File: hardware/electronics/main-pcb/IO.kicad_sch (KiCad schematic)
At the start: 22 parts, among them J1 IMU1, J2 IMU2, J3 Conn_01x04_Socket, J4 XT60-M, P1 USB_C_Plug_USB2.0, SW1 PUSH

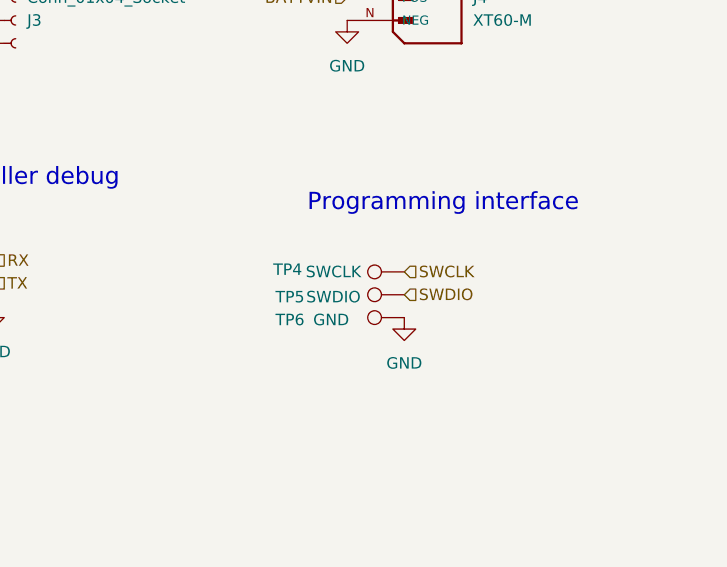
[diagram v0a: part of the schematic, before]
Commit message: worked on cmsis dap implementation aswell as cleaned up startup files for both microcontrolers
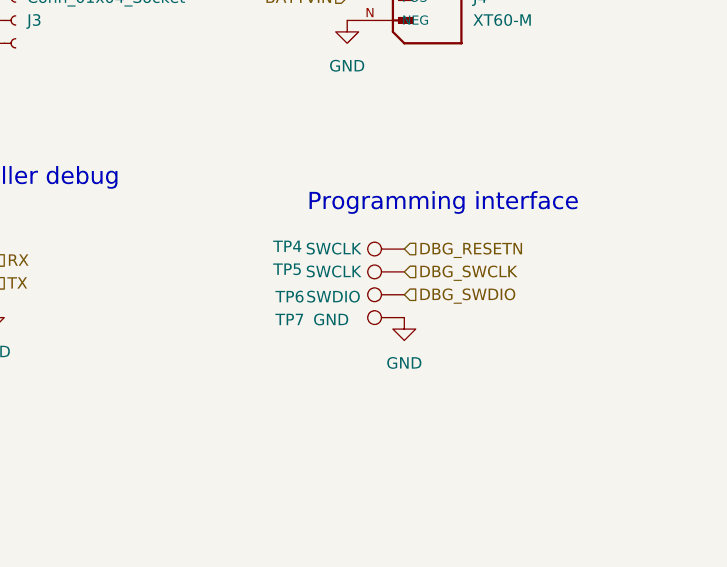
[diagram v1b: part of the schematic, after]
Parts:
- added TP4: SWCLK, TestPoint:TestPoint_Pad_D1.5mm, symbol Connector:TestPoint
- renumbered TP4 to TP5, TP5 to TP6, TP6 to TP7
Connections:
- net SWCLK renamed DBG_SWCLK
- net SWDIO renamed DBG_SWDIO
- new net DBG_RESETN: TP4.1
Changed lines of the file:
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@@
 		)
 	)
+	(hierarchical_label "DBG_RESETN"
+		(shape input)
+		(at 238.76 115.57 0)
+		(fields_autoplaced yes)
+		(effects
+			(font
+				(size 1.27 1.27)
+			)
+			(justify left)
+		)
+	)
 	(hierarchical_label "TX"
 		(shape input)
@@
 		)
 	)
-	(hierarchical_label "SWCLK"
+	(hierarchical_label "DBG_SWCLK"
 		(shape input)
 		(at 238.76 118.11 0)
@@
 		)
 	)
-	(hierarchical_label "SWDIO"
+	(hierarchical_label "DBG_SWDIO"
 		(shape input)
 		(at 238.76 120.65 0)
@@
 		(on_board yes)
 		(dnp no)
-		(property "Reference" "TP6"
+		(property "Reference" "TP7"
 			(at 226.06 123.444 90)
 			(effects
@@
 			(project "motordriver"
 				(path "/c7634e88-16d1-45ec-9aac-9c841e03cf6d/38bc72d2-c2f6-4538-9c33-e1ab2a8ac987"
-					(reference "TP6")
+					(reference "TP7")
 					(unit 1)
 				)
@@
 		(on_board yes)
 		(dnp no)
-		(property "Reference" "TP4"
+		(property "Reference" "TP5"
 			(at 225.806 117.856 90)
 			(effects
@@
 			(project "motordriver"
 				(path "/c7634e88-16d1-45ec-9aac-9c841e03cf6d/38bc72d2-c2f6-4538-9c33-e1ab2a8ac987"
-					(reference "TP4")
+					(reference "TP5")
 					(unit 1)
 				)
@@
 		(on_board yes)
 		(dnp no)
-		(property "Reference" "TP5"
+		(property "Reference" "TP6"
 			(at 226.06 120.904 90)
 			(effects
@@
 			(project "motordriver"
 				(path "/c7634e88-16d1-45ec-9aac-9c841e03cf6d/38bc72d2-c2f6-4538-9c33-e1ab2a8ac987"
-					(reference "TP5")
+					(reference "TP6")
 					(unit 1)
 				)
@@
 					(unit 1)
 				)
+			)
+		)
+	)
+	(symbol
+		(lib_id "Connector:TestPoint")
+		(at 238.76 115.57 90)
+		(unit 1)
+		(exclude_from_sim no)
+		(in_bom yes)
+		(on_board yes)
+		(dnp no)
+		(property "Reference" "TP4"
+			(at 225.806 115.316 90)
+			(effects
+				(font
+					(size 1.27 1.27)
+				)
+			)
+		)
+		(property "Value" "SWCLK"
+			(at 230.886 115.57 90)
+			(effects
+				(font
+					(size 1.27 1.27)
+				)
+			)
+		)
+		(property "Footprint" "TestPoint:TestPoint_Pad_D1.5mm"
+			(at 238.76 110.49 0)
+			(effects
+				(font
+					(size 1.27 1.27)
+				)
+				(hide yes)
+			)
+		)
+		(property "Datasheet" "~"
+			(at 238.76 110.49 0)
+			(effects
+				(font
+					(size 1.27 1.27)
+				)
+				(hide yes)
+			)
+		)
+		(property "Description" "test point"
+			(at 238.76 115.57 0)
+			(effects
+				(font
+					(size 1.27 1.27)
+				)
+				(hide yes)
+			)
+		)
+		(pin "1"
+		)
+		(instances
+			(project "motordriver"
+				(path "/c7634e88-16d1-45ec-9aac-9c841e03cf6d/38bc72d2-c2f6-4538-9c33-e1ab2a8ac987"
+					(reference "TP4")
+					(unit 1)
+				)

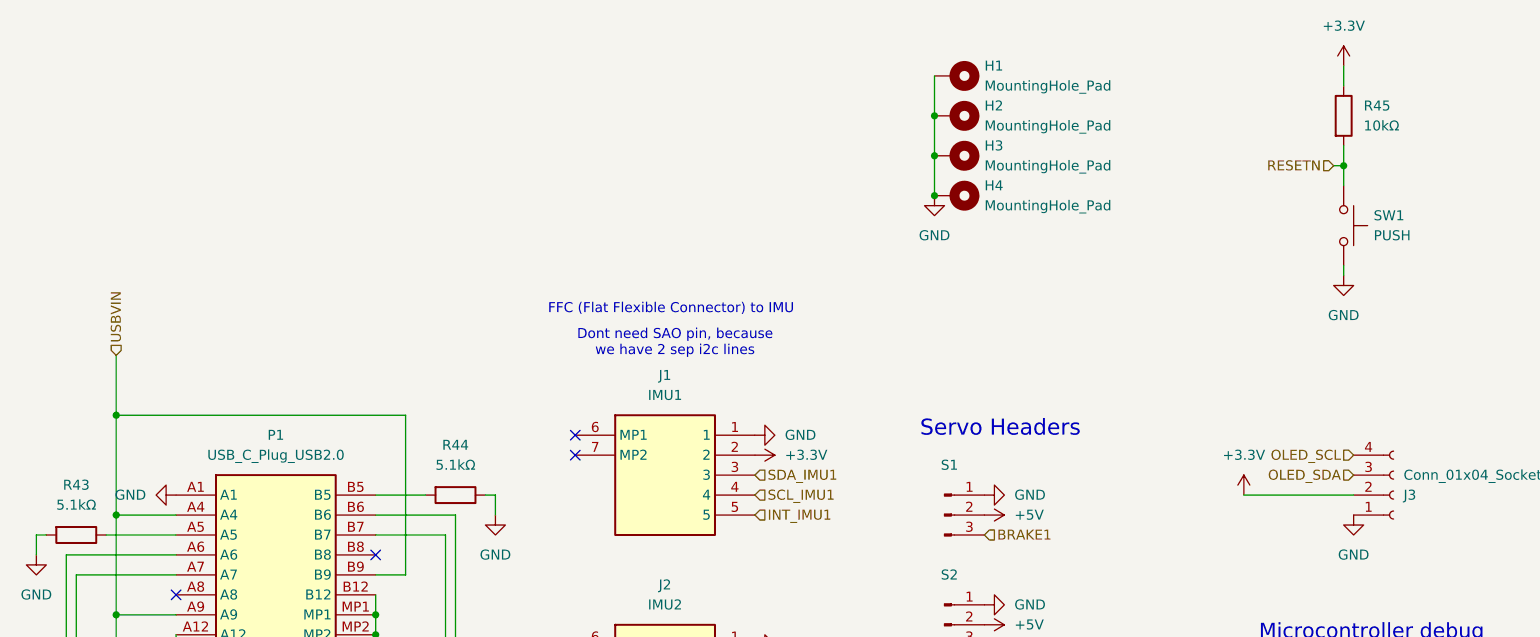
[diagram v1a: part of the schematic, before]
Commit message: added new brake chopper logic, the previous was sketchy, still we might need to find better brake resistors than the one I added
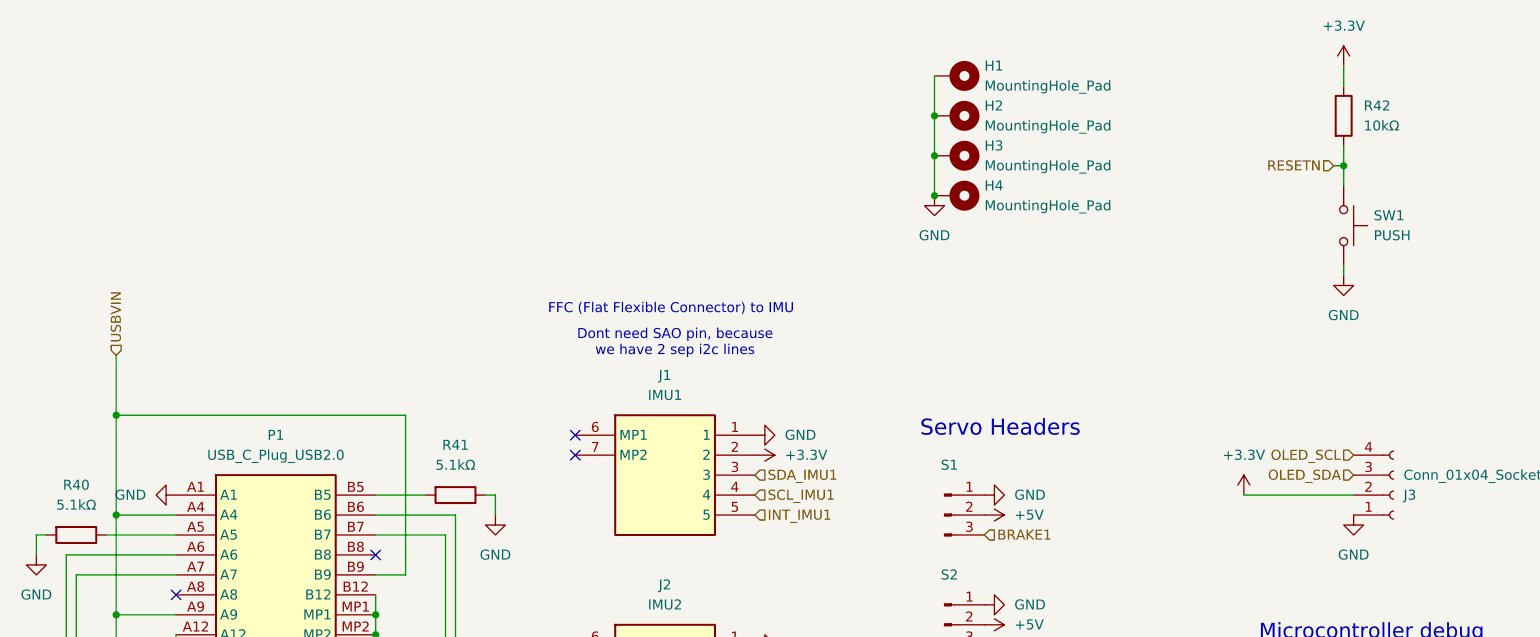
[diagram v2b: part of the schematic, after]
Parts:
- renumbered R43 to R40, R44 to R41, R45 to R42
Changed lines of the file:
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@@
 		(dnp no)
 		(fields_autoplaced yes)
-		(property "Reference" "#PWR076"
+		(property "Reference" "#PWR072"
 			(at 139.7 92.71 0)
 			(effects
@@
 			(project "motordriver"
 				(path "/c7634e88-16d1-45ec-9aac-9c841e03cf6d/38bc72d2-c2f6-4538-9c33-e1ab2a8ac987"
-					(reference "#PWR076")
+					(reference "#PWR072")
 					(unit 1)
 				)
@@
 		(dnp no)
 		(fields_autoplaced yes)
-		(property "Reference" "#PWR082"
+		(property "Reference" "#PWR078"
 			(at 189.23 39.37 0)
 			(effects
@@
 			(project ""
 				(path "/c7634e88-16d1-45ec-9aac-9c841e03cf6d/38bc72d2-c2f6-4538-9c33-e1ab2a8ac987"
-					(reference "#PWR082")
+					(reference "#PWR078")
 					(unit 1)
 				)
@@
 		(dnp no)
 		(fields_autoplaced yes)
-		(property "Reference" "#PWR069"
+		(property "Reference" "#PWR065"
 			(at 81.28 99.06 0)
 			(effects
@@
 			(project "motordriver"
 				(path "/c7634e88-16d1-45ec-9aac-9c841e03cf6d/38bc72d2-c2f6-4538-9c33-e1ab2a8ac987"
-					(reference "#PWR069")
+					(reference "#PWR065")
 					(unit 1)
 				)
@@
 		(dnp no)
 		(fields_autoplaced yes)
-		(property "Reference" "#PWR074"
+		(property "Reference" "#PWR070"
 			(at 137.16 58.42 0)
 			(effects
@@
 			(project "motordriver"
 				(path "/c7634e88-16d1-45ec-9aac-9c841e03cf6d/38bc72d2-c2f6-4538-9c33-e1ab2a8ac987"
-					(reference "#PWR074")
+					(reference "#PWR070")
 					(unit 1)
 				)
@@
 		(dnp no)
 		(fields_autoplaced yes)
-		(property "Reference" "#PWR075"
+		(property "Reference" "#PWR071"
 			(at 149.86 90.17 0)
 			(effects
@@
 			(project "motordriver"
 				(path "/c7634e88-16d1-45ec-9aac-9c841e03cf6d/38bc72d2-c2f6-4538-9c33-e1ab2a8ac987"
-					(reference "#PWR075")
+					(reference "#PWR071")
 					(unit 1)
 				)
@@
 		(dnp no)
 		(fields_autoplaced yes)
-		(property "Reference" "R45"
+		(property "Reference" "R42"
 			(at 191.77 40.6399 0)
 			(effects
@@
 			(project ""
 				(path "/c7634e88-16d1-45ec-9aac-9c841e03cf6d/38bc72d2-c2f6-4538-9c33-e1ab2a8ac987"
-					(reference "R45")
+					(reference "R42")
 					(unit 1)
 				)
@@
 		(dnp no)
 		(fields_autoplaced yes)
-		(property "Reference" "#PWR078"
+		(property "Reference" "#PWR074"
 			(at 139.7 106.68 0)
 			(effects
@@
 			(project "motordriver"
 				(path "/c7634e88-16d1-45ec-9aac-9c841e03cf6d/38bc72d2-c2f6-4538-9c33-e1ab2a8ac987"
-					(reference "#PWR078")
+					(reference "#PWR074")
 					(unit 1)
 				)
@@
 		(on_board yes)
 		(dnp no)
-		(property "Reference" "#PWR072"
+		(property "Reference" "#PWR068"
 			(at 120.65 109.22 0)
 			(effects
@@
 			(project "motordriver"
 				(path "/c7634e88-16d1-45ec-9aac-9c841e03cf6d/38bc72d2-c2f6-4538-9c33-e1ab2a8ac987"
-					(reference "#PWR072")
+					(reference "#PWR068")
 					(unit 1)
 				)
@@
 		(dnp no)
 		(fields_autoplaced yes)
-		(property "Reference" "#PWR085"
+		(property "Reference" "#PWR081"
 			(at 193.04 128.27 0)
 			(effects
@@
 			(project "motordriver"
 				(path "/c7634e88-16d1-45ec-9aac-9c841e03cf6d/38bc72d2-c2f6-4538-9c33-e1ab2a8ac987"
-					(reference "#PWR085")
+					(reference "#PWR081")
 					(unit 1)
 				)
@@
 		(dnp no)
 		(fields_autoplaced yes)
-		(property "Reference" "#PWR084"
+		(property "Reference" "#PWR080"
 			(at 190.5 99.06 0)
 			(effects
@@
 			(project "motordriver"
 				(path "/c7634e88-16d1-45ec-9aac-9c841e03cf6d/38bc72d2-c2f6-4538-9c33-e1ab2a8ac987"
-					(reference "#PWR084")
+					(reference "#PWR080")
 					(unit 1)
 				)
@@
 		(dnp no)
 		(fields_autoplaced yes)
-		(property "Reference" "#PWR068"
+		(property "Reference" "#PWR064"
 			(at 72.39 113.03 0)
 			(effects
@@
 			(project "motordriver"
 				(path "/c7634e88-16d1-45ec-9aac-9c841e03cf6d/38bc72d2-c2f6-4538-9c33-e1ab2a8ac987"
-					(reference "#PWR068")
+					(reference "#PWR064")
 					(unit 1)
 				)
@@
 		(dnp no)
 		(fields_autoplaced yes)
-		(property "Reference" "#PWR079"
+		(property "Reference" "#PWR075"
 			(at 149.86 118.11 0)
 			(effects
@@
 			(project "motordriver"
 				(path "/c7634e88-16d1-45ec-9aac-9c841e03cf6d/38bc72d2-c2f6-4538-9c33-e1ab2a8ac987"
-					(reference "#PWR079")
+					(reference "#PWR075")
 					(unit 1)
 				)
@@
 		(dnp no)
 		(fields_autoplaced yes)
-		(property "Reference" "#PWR080"
+		(property "Reference" "#PWR076"
 			(at 139.7 120.65 0)
 			(effects
@@
 			(project "motordriver"
 				(path "/c7634e88-16d1-45ec-9aac-9c841e03cf6d/38bc72d2-c2f6-4538-9c33-e1ab2a8ac987"
-					(reference "#PWR080")
+					(reference "#PWR076")
 					(unit 1)
 				)
@@
 		(dnp no)
 		(fields_autoplaced yes)
-		(property "Reference" "#PWR077"
+		(property "Reference" "#PWR073"
 			(at 149.86 104.14 0)
 			(effects
@@
 			(project "motordriver"
 				(path "/c7634e88-16d1-45ec-9aac-9c841e03cf6d/38bc72d2-c2f6-4538-9c33-e1ab2a8ac987"
-					(reference "#PWR077")
+					(reference "#PWR073")
 					(unit 1)
 				)
@@
 		(dnp no)
 		(fields_autoplaced yes)
-		(property "Reference" "R44"
+		(property "Reference" "R41"
 			(at 76.2 83.82 90)
 			(effects
@@
 			(project "motordriver"
 				(path "/c7634e88-16d1-45ec-9aac-9c841e03cf6d/38bc72d2-c2f6-4538-9c33-e1ab2a8ac987"
-					(reference "R44")
+					(reference "R41")
 					(unit 1)
 				)
@@
 		(dnp no)
 		(fields_autoplaced yes)
-		(property "Reference" "#PWR086"
+		(property "Reference" "#PWR082"
 			(at 232.41 96.52 0)
 			(effects
@@
 			(project "motordriver"
 				(path "/c7634e88-16d1-45ec-9aac-9c841e03cf6d/38bc72d2-c2f6-4538-9c33-e1ab2a8ac987"
-					(reference "#PWR086")
+					(reference "#PWR082")
 					(unit 1)
 				)
@@
 		(dnp no)
 		(fields_autoplaced yes)
-		(property "Reference" "#PWR087"
+		(property "Reference" "#PWR083"
 			(at 238.76 129.54 0)
 			(effects
@@
 			(project "motordriver"
 				(path "/c7634e88-16d1-45ec-9aac-9c841e03cf6d/38bc72d2-c2f6-4538-9c33-e1ab2a8ac987"
-					(reference "#PWR087")
+					(reference "#PWR083")
 					(unit 1)
 				)
@@
 		(dnp no)
 		(fields_autoplaced yes)
-		(property "Reference" "#PWR083"
+		(property "Reference" "#PWR079"
 			(at 189.23 68.58 0)
 			(effects
@@
 			(project ""
 				(path "/c7634e88-16d1-45ec-9aac-9c841e03cf6d/38bc72d2-c2f6-4538-9c33-e1ab2a8ac987"
-					(reference "#PWR083")
+					(reference "#PWR079")
 					(unit 1)
 				)
@@
 		(on_board yes)
 		(dnp no)
-		(property "Reference" "#PWR073"
+		(property "Reference" "#PWR069"
 			(at 110.49 111.76 0)
 			(effects
@@
 			(project "motordriver"
 				(path "/c7634e88-16d1-45ec-9aac-9c841e03cf6d/38bc72d2-c2f6-4538-9c33-e1ab2a8ac987"
-					(reference "#PWR073")
+					(reference "#PWR069")
 					(unit 1)
 				)
@@
 		(dnp no)
 		(fields_autoplaced yes)
-		(property "Reference" "R43"
+		(property "Reference" "R40"
 			(at 27.94 88.9 90)
 			(effects
@@
 			(project "motordriver"
 				(path "/c7634e88-16d1-45ec-9aac-9c841e03cf6d/38bc72d2-c2f6-4538-9c33-e1ab2a8ac987"
-					(reference "R43")
+					(reference "R40")
 					(unit 1)
 				)
@@
 		(on_board yes)
 		(dnp no)
-		(property "Reference" "#PWR070"
+		(property "Reference" "#PWR066"
 			(at 120.65 82.55 0)
 			(effects
@@
 			(project "motordriver"
 				(path "/c7634e88-16d1-45ec-9aac-9c841e03cf6d/38bc72d2-c2f6-4538-9c33-e1ab2a8ac987"
-					(reference "#PWR070")
+					(reference "#PWR066")
 					(unit 1)
 				)
@@
 		(dnp no)
 		(fields_autoplaced yes)
-		(property "Reference" "#PWR067"
+		(property "Reference" "#PWR063"
 			(at 34.29 110.49 0)
 			(effects
@@
 			(project "motordriver"
 				(path "/c7634e88-16d1-45ec-9aac-9c841e03cf6d/38bc72d2-c2f6-4538-9c33-e1ab2a8ac987"
-					(reference "#PWR067")
+					(reference "#PWR063")
 					(unit 1)
 				)
@@
 		(dnp no)
 		(fields_autoplaced yes)
-		(property "Reference" "#PWR066"
+		(property "Reference" "#PWR062"
 			(at 34.29 90.17 0)
 			(effects
@@
 			(project "motordriver"
 				(path "/c7634e88-16d1-45ec-9aac-9c841e03cf6d/38bc72d2-c2f6-4538-9c33-e1ab2a8ac987"
-					(reference "#PWR066")
+					(reference "#PWR062")
 					(unit 1)
 				)
@@
 		(dnp no)
 		(fields_autoplaced yes)
-		(property "Reference" "#PWR081"
+		(property "Reference" "#PWR077"
 			(at 176.53 93.98 0)
 			(effects
@@
 			(project "motordriver"
 				(path "/c7634e88-16d1-45ec-9aac-9c841e03cf6d/38bc72d2-c2f6-4538-9c33-e1ab2a8ac987"
-					(reference "#PWR081")
+					(reference "#PWR077")
 					(unit 1)
 				)
@@
 		(dnp no)
 		(fields_autoplaced yes)
-		(property "Reference" "#PWR065"
+		(property "Reference" "#PWR061"
 			(at 22.86 104.14 0)
 			(effects
@@
 			(project "motordriver"
 				(path "/c7634e88-16d1-45ec-9aac-9c841e03cf6d/38bc72d2-c2f6-4538-9c33-e1ab2a8ac987"
-					(reference "#PWR065")
+					(reference "#PWR061")
 					(unit 1)
 				)
@@
 		(on_board yes)
 		(dnp no)
-		(property "Reference" "#PWR071"
+		(property "Reference" "#PWR067"
 			(at 110.49 85.09 0)
 			(effects
@@
 			(project "motordriver"
 				(path "/c7634e88-16d1-45ec-9aac-9c841e03cf6d/38bc72d2-c2f6-4538-9c33-e1ab2a8ac987"
-					(reference "#PWR071")
+					(reference "#PWR067")
 					(unit 1)
 				)
